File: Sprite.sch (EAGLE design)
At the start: 28 parts, among them P1 SPRITE_PIN, P2 SPRITE_PIN, U1 CC430F5137, U2 LSM9DS1, X1 TCXO_7Z

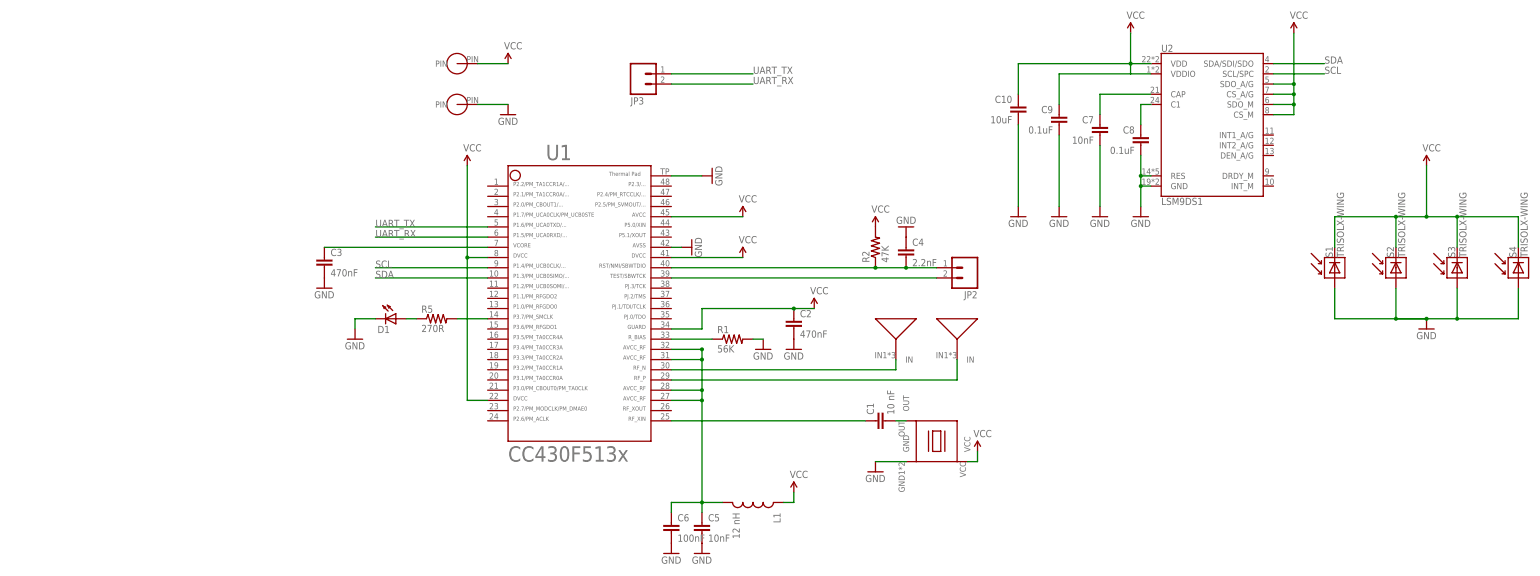
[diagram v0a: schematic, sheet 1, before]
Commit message: moved solar cells + antenna on new board
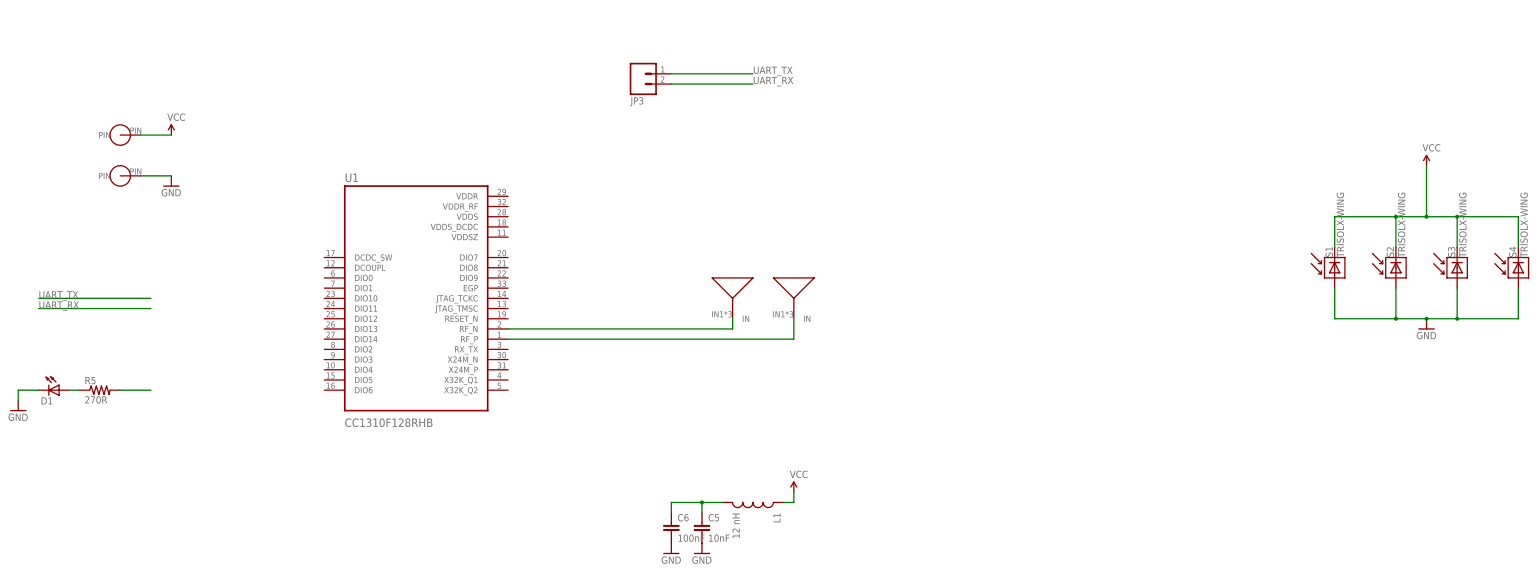
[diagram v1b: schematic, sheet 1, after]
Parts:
- removed C1: 10 nF, SparkFun:CAP0603-CAP
- removed C10: 10uF, SparkFun:CAP0603-CAP
- removed C2, C3: 470nF, SparkFun:CAP0603-CAP
- removed C4: 2.2nF, SparkFun:CAP0603-CAP
- removed C7: 10nF, SparkFun:CAP0603-CAP
- removed C8, C9: 0.1uF, SparkFun:CAP0603-CAP
- removed JP2: (no value), SparkFun:M02PTH
- removed R1: 56K, SparkFun:RESISTOR0603-RES
- removed R2: 47K, SparkFun:RESISTOR0603-RES
- removed U2: LSM9DS1, LSM9DS1:LSM9DS1
- removed X1: TCXO_7Z, SpriteTCXO:TCXO_7Z
- U1: value CC430F5137 -> CC1310F128RHB; device TI_MSP430_v16:CC430F513X---RGZ48 -> CC1310F128RHB:CC1310F128RHB
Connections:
- removed net N$1: C1.1, U1.25
- removed net N$12: C1.2, X1.OUT
- removed net N$3: R1.1, U1.33
- removed net N$4: C3.1, U1.7
- removed net N$5: C7.1, U2.CAP
- removed net N$6: C8.1, U2.C1
- removed net RST: C4.2, JP2.1, R2.1, U1.40
- removed net SCL: U1.9, U2.SCL/SPC
- removed net SDA: U1.10, U2.SDA/SDI/SDO
- removed net TEST: JP2.2, U1.39
- net GND: now also P2.PIN; no longer C10.2, C2.2, C3.2, C4.1, C7.2, C8.2, C9.2, P1.PIN, R1.2, U1.42, U1.49, U2.GND, U2.RES, X1.GND
- net N$2: no longer U1.14
- net RFN: now also U1.RF_N; no longer U1.30
- net RFP: now also U1.RF_P; no longer U1.29
- net UART_RX: no longer U1.6
- net UART_TX: no longer U1.5
- net VCC: now also P1.PIN; no longer C10.1, C2.1, C9.1, P2.PIN, R2.2, U1.22, U1.34, U1.41, U1.45, U1.8, U2.CS_A/G, U2.CS_M, U2.SDO_A/G, U2.SDO_M, U2.VDD, U2.VDDIO, X1.VCC
- net VCCRF: no longer U1.27, U1.28, U1.31, U1.32
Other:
- moved on the sheet: D1, R5
